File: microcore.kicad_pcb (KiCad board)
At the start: 4 copper layers, 90 x 60 mm, 0 parts

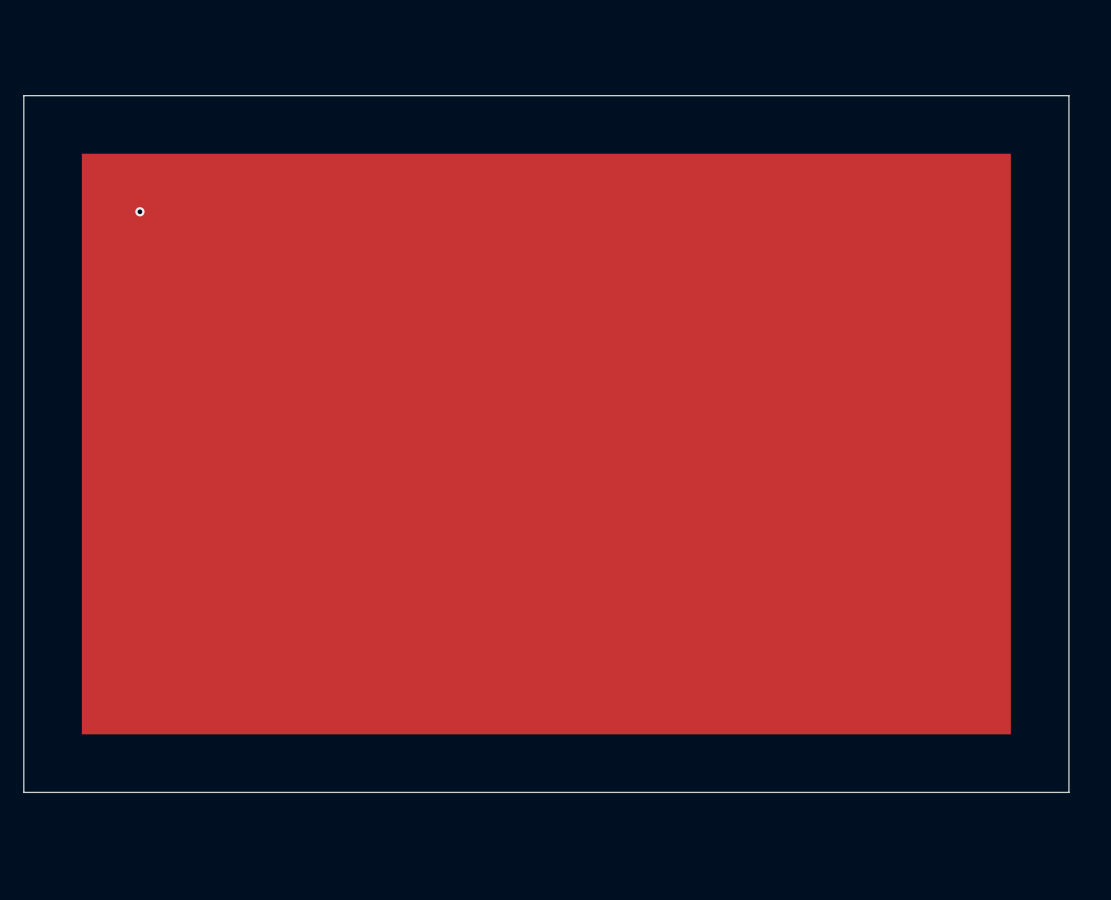
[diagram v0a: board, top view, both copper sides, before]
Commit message: Add first real Micro Core modules (rev b)
Place mega-mcu100/0.3, power_12and5V/0.3, vr-discrete/0.5 and TE 776231-1
on the 90x60 frame; add INJ4/LS3/ANALOG/HALL hierarchy with DPAK drivers.
Bump BOARD_REVISION to b so Create Board writes boards/microcore-b/.
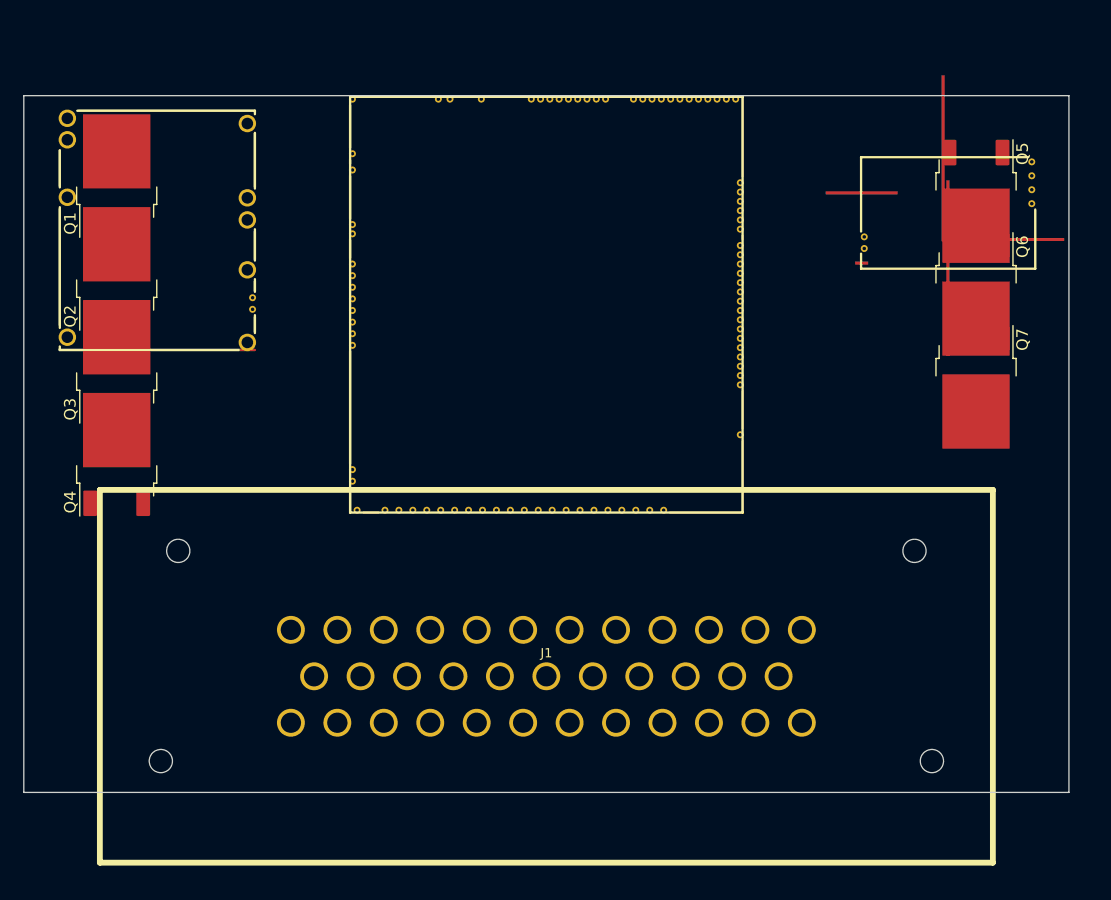
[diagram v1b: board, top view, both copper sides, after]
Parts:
- added J1: TE_776231-1, kicad6-libraries:TE_776231, F.Cu at (45.0, 50.0)
- added M1: Module:mega-mcu100/0.3, hellen-one-mega-mcu100-0.3:mega-mcu100, F.Cu at (28.0, 36.0)
- added M2: Module-power_12and5V-0.3, hellen-one-power_12and5V-0.3:power_12and5V, F.Cu at (3.00, 22.0)
- added M3: Module-vr-discrete-0.5, hellen-one-vr-discrete-0.5:vr-discrete, F.Cu at (72.0, 15.0)
- added Q1: VND14NV04-E, hellen-one-common:DPAK, F.Cu at (8.00, 8.00)
- added Q2: VND14NV04-E, hellen-one-common:DPAK, F.Cu at (8.00, 16.0)
- added Q3: VND14NV04-E, hellen-one-common:DPAK, F.Cu at (8.00, 24.0)
- added Q4: VND14NV04-E, hellen-one-common:DPAK, F.Cu at (8.00, 32.0)
- added Q5: VND14NV04-E, hellen-one-common:DPAK, F.Cu at (82.0, 8.00)
- added Q6: VND14NV04-E, hellen-one-common:DPAK, F.Cu at (82.0, 16.0)
- added Q7: VND14NV04-E, hellen-one-common:DPAK, F.Cu at (82.0, 24.0)
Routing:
- net (no net): vias 1 -> 0
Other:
- board text added: "Micro Core rev B 90x60 4-layer mega-mcu100/0.3 + power + VR TE 776231-1 south"
- board text removed: "Micro Core scaffold 90 x 60 mm outline aux_axis_origin 0,0 (bottom-left) Place Hellen modules next"

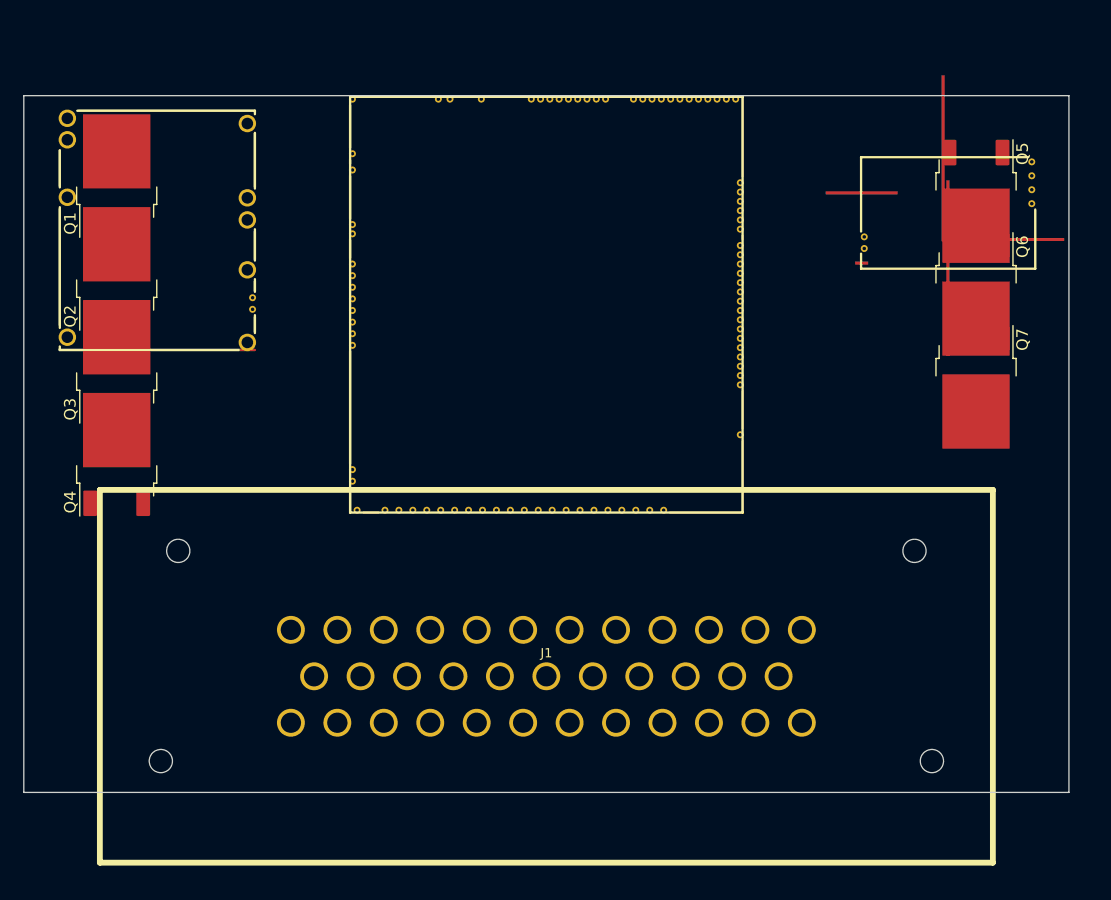
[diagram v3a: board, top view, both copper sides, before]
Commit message: Inset module footprints; drop frame DPAKs for gerbmerge
Keep mega/power/VR + AMPSEAL on PCB with margin from Edge.Cuts so
rectangular pad trim does not hit gerbmerge float&int bug. DPAKs remain
on INJ4/LS3 schematics for the next placement pass.
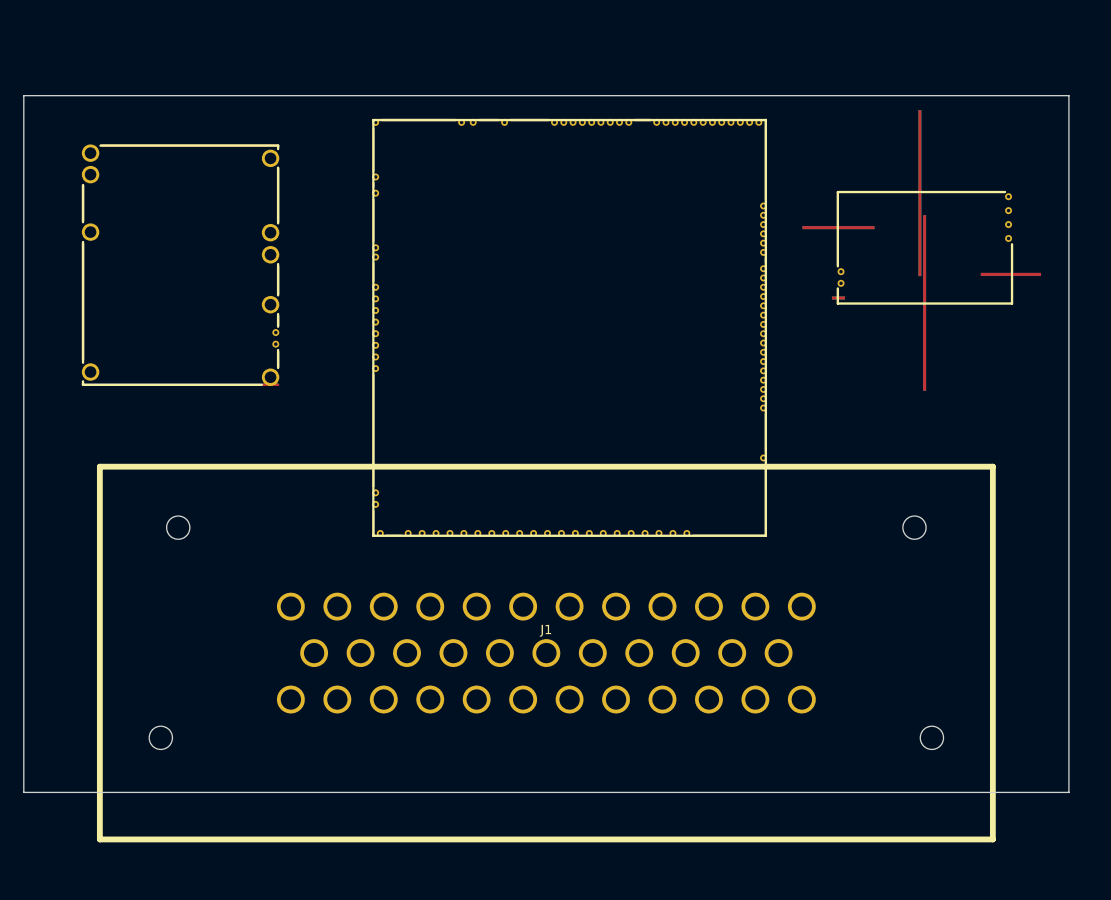
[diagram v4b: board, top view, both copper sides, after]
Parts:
- removed Q1, Q2, Q3, Q4, Q5, Q6, Q7: VND14NV04-E, hellen-one-common:DPAK
- moved M2 3.61 mm to (5.00, 25.0)
- moved M3 3.61 mm to (70.0, 18.0)
- moved M1 2.83 mm to (30.0, 38.0)
- moved J1 2.00 mm to (45.0, 48.0)

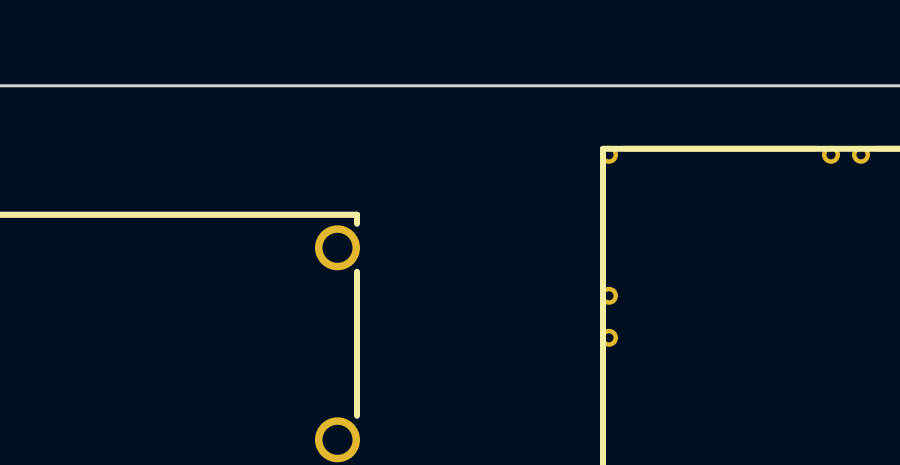
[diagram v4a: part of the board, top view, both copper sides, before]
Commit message: Swap VR to max9924/0.3; add frame USB Mini-B; bump rev c
Replace vr-discrete/0.5 with vr-max9924/0.3 (east of MCU), keep VR± on
AMPSEAL 28/29. Add hellen-one-common USB_B_Mini (USB-MINI-B-VERTICAL) on
the north edge wired to mega-mcu100 USBM/USBP/USBID + VBUS/GND. Bump
BOARD_REVISION to c after Create Board already produced rev b on this branch.
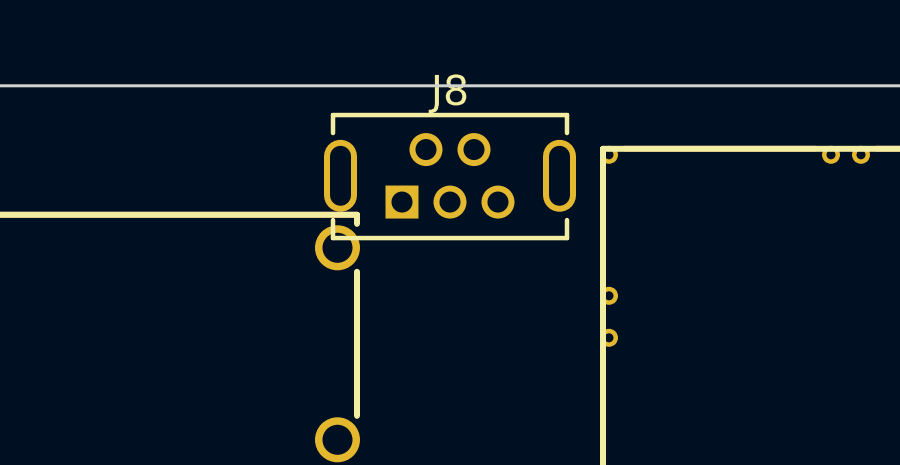
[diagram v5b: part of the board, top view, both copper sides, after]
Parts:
- added J8: USB_B_Mini, hellen-one-common:USB-MINI-B-VERTICAL, F.Cu at (25.0, 3.00)
- M3: value Module-vr-discrete-0.5 -> Module-vr-max9924-0.3; footprint hellen-one-vr-discrete-0.5:vr-discrete -> hellen-one-vr-max9924-0.3:vr-max9924
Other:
- board text added: "Micro Core rev C 90x60 4-layer mega-mcu100/0.3 + power + vr-max9924/0.3 USB Mini-B north + TE 776231-1 south"
- board text removed: "Micro Core rev B 90x60 4-layer mega-mcu100/0.3 + power + VR TE 776231-1 south"
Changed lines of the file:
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@@
 		(title "Micro Core")
 		(date "2026-09-13")
-		(rev "B")
+		(rev "C")
 		(company "Core EFI")
-		(comment 1 "modules-v1: mega-mcu100 + power + VR + AMPSEAL")
+		(comment 1 "modules-v1: mega-mcu100 + power + vr-max9924 + USB Mini-B + AMPSEAL")
 	)
 	(layers
@@
 		(layer "Edge.Cuts")
 	)
-	(gr_text "Micro Core rev B\n90x60 4-layer\nmega-mcu100/0.3 + power + VR\nTE 776231-1 south"
+	(gr_text "Micro Core rev C\n90x60 4-layer\nmega-mcu100/0.3 + power + vr-max9924/0.3\nUSB Mini-B north + TE 776231-1 south"
 		(at 45 5 0)
 		(layer "Cmts.User")
@@
 		)
 	)
-	(footprint "hellen-one-vr-discrete-0.5:vr-discrete"
+	(footprint "hellen-one-vr-max9924-0.3:vr-max9924"
 		(layer "F.Cu")
 		(at 70 18)
@@
 			)
 		)
-		(property "Value" "Module-vr-discrete-0.5"
+		(property "Value" "Module-vr-max9924-0.3"
 			(at 9.02 -16 -90)
 			(unlocked yes)
@@
 			)
 		)
-		(property "Footprint" "hellen-one-vr-discrete-0.5:vr-discrete"
+		(property "Footprint" "hellen-one-vr-max9924-0.3:vr-max9924"
 			(at 0 0 -90)
 			(layer "F.Fab")
@@
 		)
 )
+	(footprint "hellen-one-common:USB-MINI-B-VERTICAL"
+		(layer "F.Cu")
+		(at 25.0 3.0)
+		(descr "http://www.tensility.com/pdffiles/54-00023.pdf")
+		(tags "usb mini receptacle vertical")
+		(property "Reference" "J8"
+			(at 0 -2.825 0)
+			(layer "F.SilkS")
+			(effects
+				(font
+					(size 1 1)
+					(thickness 0.15)
+				)
+			)
+		)
+		(property "Value" "USB_B_Mini"
+			(at -0.1 3.075 0)
+			(layer "F.Fab")
+			(effects
+				(font
+					(size 1 1)
+					(thickness 0.15)
+				)
+			)
+		)
+		(property "Footprint" "hellen-one-common:USB-MINI-B-VERTICAL"
+			(at 0 0 0)
+			(layer "F.Fab")
+			(hide yes)
+			(effects
+				(font
+					(size 1.27 1.27)
+				)
+			)
+		)
+		(property "Datasheet" "~"
+			(at 0 0 0)
+			(layer "F.Fab")
+			(hide yes)
+			(effects
+				(font
+					(size 1.27 1.27)
+				)
+			)
+		)
+		(property "LCSC" "C13453"
+			(at 0 0 0)
+			(layer "F.Fab")
+			(hide yes)
+			(effects
+				(font
+					(size 1.27 1.27)
+				)
+			)
+		)
+		(attr through_hole)
+		(fp_line
+			(start 3.9 -2.025)
+			(end 3.9 -1.425)
+			(stroke
+				(width 0.15)
+				(type solid)
+			)
+			(layer "F.SilkS")
+		)
+		(fp_line
+			(start -3.9 -2.025)
+			(end 3.9 -2.025)
+			(stroke
+				(width 0.15)
+				(type solid)
+			)
+			(layer "F.SilkS")
+		)
+		(fp_line
+			(start -3.9 -1.425)
+			(end -3.9 -2.025)
+			(stroke
+				(width 0.15)
+				(type solid)
+			)
+			(layer "F.SilkS")
+		)
+		(fp_line
+			(start -3.9 1.475)
+			(end -3.9 2.075)
+			(stroke
+				(width 0.15)
+				(type solid)
+			)
+			(layer "F.SilkS")
+		)
+		(fp_line
+			(start 3.9 2.075)
+			(end 3.9 1.475)
+			(stroke
+				(width 0.15)
+				(type solid)
+			)
+			(layer "F.SilkS")
+		)
+		(fp_line
+			(start 3.9 2.075)
+			(end -3.9 2.075)
+			(stroke
+				(width 0.15)
+				(type solid)
+			)
+			(layer "F.SilkS")
+		)
+		(fp_line
+			(start -3.75 -2.125)
+			(end -3.75 2.125)
+			(stroke
+				(width 0.05)
+				(type solid)
+			)
+			(layer "F.CrtYd")
+		)
+		(fp_line
+			(start 3.75 -2.125)
+			(end -3.75 -2.125)
+			(stroke
+				(width 0.05)
+				(type solid)
+			)
+			(layer "F.CrtYd")
+		)
+		(fp_line
+			(start 3.75 2.125)
+			(end 3.75 -2.125)
+			(stroke
+				(width 0.05)
+				(type solid)
+			)
+			(layer "F.CrtYd")
+		)
+		(fp_line
+			(start -3.75 2.125)
+			(end 3.75 2.125)
+			(stroke
+				(width 0.05)
+				(type solid)
+			)
+			(layer "F.CrtYd")
+		)
+		(pad "1" thru_hole rect
+			(at -1.6 0.875)
+			(size 1.1 1.1)
+			(drill 0.7)
+			(layers "*.Cu" "*.Mask")
+			(net 0 "")
+		)
+		(pad "2" thru_hole circle
+			(at -0.8 -0.875)
+			(size 1.1 1.1)
+			(drill 0.7)
+			(layers "*.Cu" "*.Mask")
+			(net 0 "")
+		)
+		(pad "3" thru_hole circle
+			(at 0 0.875)
+			(size 1.1 1.1)
+			(drill 0.7)
+			(layers "*.Cu" "*.Mask")
+			(net 0 "")
+		)
+		(pad "4" thru_hole circle
+			(at 0.8 -0.875)
+			(size 1.1 1.1)
+			(drill 0.7)
+			(layers "*.Cu" "*.Mask")
+			(net 0 "")
+		)
+		(pad "5" thru_hole circle
+			(at 1.6 0.875)
+			(size 1.1 1.1)
+			(drill 0.7)
+			(layers "*.Cu" "*.Mask")
+			(net 0 "")
+		)
+		(pad "6" thru_hole oval
+			(at 3.65 0)
+			(size 1.1 2.4)
+			(drill oval 0.7 2)
+			(layers "*.Cu" "*.Mask")
+			(net 0 "")
+		)
+		(pad "6" thru_hole oval
+			(at -3.65 0)
+			(size 1.1 2.4)
+			(drill oval 0.7 2)
+			(layers "*.Cu" "*.Mask")
+			(net 0 "")
+		)
+	)
 )

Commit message: Freeze AMPSEAL spare pins and add frame BOOT/RESET (rev d)
Assign pins 11/26/30–35 to DIN1–2, IGN5–8, SGND, PGND; wire to mega.
Add gasketed SW_BOOT (BOOT0–V33) and SW_RESET (nReset–GND) near USB.
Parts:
- added SW_BOOT: Button_SPST, hellen-one-common:SMD-2_2.9x3.9x1.7, F.Cu at (40.0, 5.00)
- added SW_RESET: Button_SPST, hellen-one-common:SMD-2_2.9x3.9x1.7, F.Cu at (50.0, 5.00)
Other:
- board text added: "Micro Core rev D 90x60 4-layer mega-mcu100/0.3 + power + vr-max9924/0.3 USB Mini-B + SW_BOOT/SW_RESET north + TE 776231-1 south"
- board text removed: "Micro Core rev C 90x60 4-layer mega-mcu100/0.3 + power + vr-max9924/0.3 USB Mini-B north + TE 776231-1 south"

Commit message: Align frame button BOM comment with mega BTN (C115357)
Create Board failed: Comment mismatch for C115357 Button_SPST vs BTN.
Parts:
- SW_BOOT, SW_RESET: value Button_SPST -> BTN
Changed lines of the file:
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@@
 			)
 		)
-		(property "Value" "Button_SPST"
+		(property "Value" "BTN"
 			(at 0 2.6 0)
 			(layer "F.Fab")
@@
 			)
 		)
-		(property "Value" "Button_SPST"
+		(property "Value" "BTN"
 			(at 0 2.6 0)
 			(layer "F.Fab")
